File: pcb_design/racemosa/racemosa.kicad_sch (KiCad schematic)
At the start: 4 parts, among them J1 USB_C_Receptacle, J2 USB_C_Receptacle

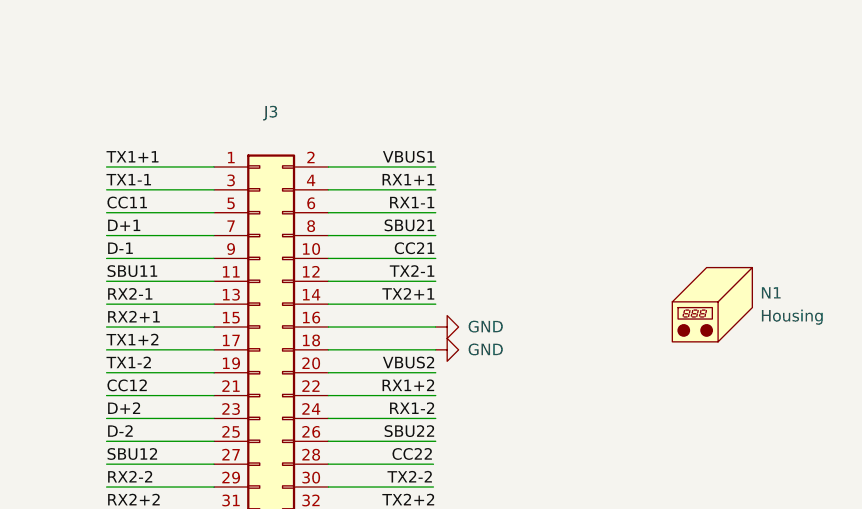
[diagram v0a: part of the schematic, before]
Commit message: Redesign for improved mounting hole placement.
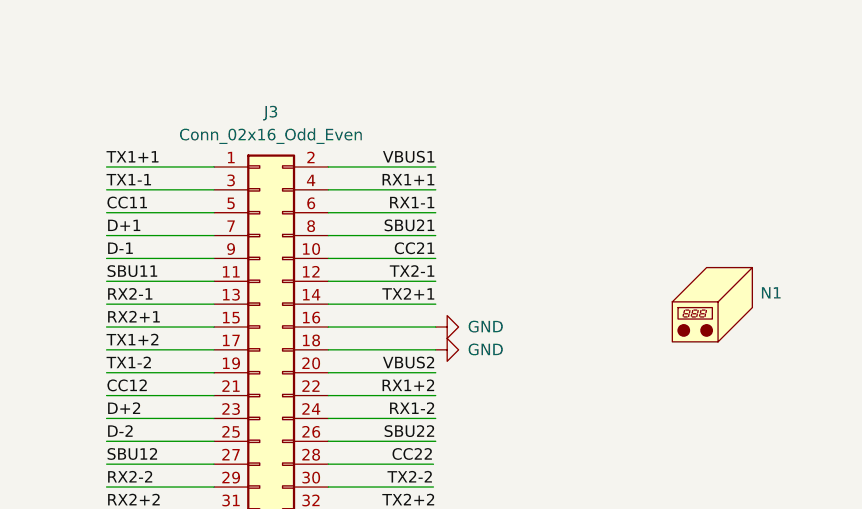
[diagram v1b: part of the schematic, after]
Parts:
- J3: value (none) -> Conn_02x16_Odd_Even; footprint (none) -> Connector_PinHeader_2.54mm:PinHeader_2x16_P2.54mm_Vertical
- N1: value Housing -> (none); footprint custom_footprints:Enclosure-Gloxinia_small -> (none)
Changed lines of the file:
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@@
       (effects (font (size 1.27 1.27)) (justify left))
     )
-    (property "Value" "Housing" (id 1) (at 229.87 62.2934 0)
+    (property "Value" "" (id 1) (at 229.87 62.2934 0)
       (effects (font (size 1.27 1.27)) (justify left))
     )
-    (property "Footprint" "custom_footprints:Enclosure-Gloxinia_small" (id 2) (at 227.076 59.436 0)
+    (property "Footprint" "" (id 2) (at 227.076 59.436 0)
       (effects (font (size 1.27 1.27)) hide)
     )
@@
     (in_bom yes) (on_board yes) (fields_autoplaced)
     (property "Reference" "J3" (id 0) (at 175.514 39.624 0))
-    (property "Value" "" (id 1) (at 175.514 42.164 0))
-    (property "Footprint" "" (id 2) (at 174.244 63.5 0)
+    (property "Value" "Conn_02x16_Odd_Even" (id 1) (at 175.514 42.164 0))
+    (property "Footprint" "Connector_PinHeader_2.54mm:PinHeader_2x16_P2.54mm_Vertical" (id 2) (at 174.244 63.5 0)
       (effects (font (size 1.27 1.27)) hide)
     )
@@
   (symbol (lib_id "power:GND") (at 193.802 66.04 90) (unit 1)
     (in_bom yes) (on_board yes) (fields_autoplaced)
-    (property "Reference" "#PWR?" (id 0) (at 200.152 66.04 0)
+    (property "Reference" "#PWR0101" (id 0) (at 200.152 66.04 0)
       (effects (font (size 1.27 1.27)) hide)
     )
@@
     )
     (path "/ebece5df-52c9-4bcb-9823-936d87818fa5"
-      (reference "#PWR?") (unit 1) (value "GND") (footprint "")
+      (reference "#PWR0101") (unit 1) (value "GND") (footprint "")
     )
     (path "/a7e4ee7d-cc20-4e93-9f3d-d257d055e4ba"
@@
     )
     (path "/3a89bb2a-ccf9-421b-8cf5-74b2caf376f9"
-      (reference "N1") (unit 1) (value "Housing") (footprint "custom_footprints:Enclosure-Gloxinia_small")
-    )
-  )
+      (reference "N1") (unit 1) (value "Housing") (footprint "custom_footprints:Enclosure-Gloxinia2_lr")
+    )
+  )
